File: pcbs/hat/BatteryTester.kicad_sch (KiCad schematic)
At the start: 21 parts

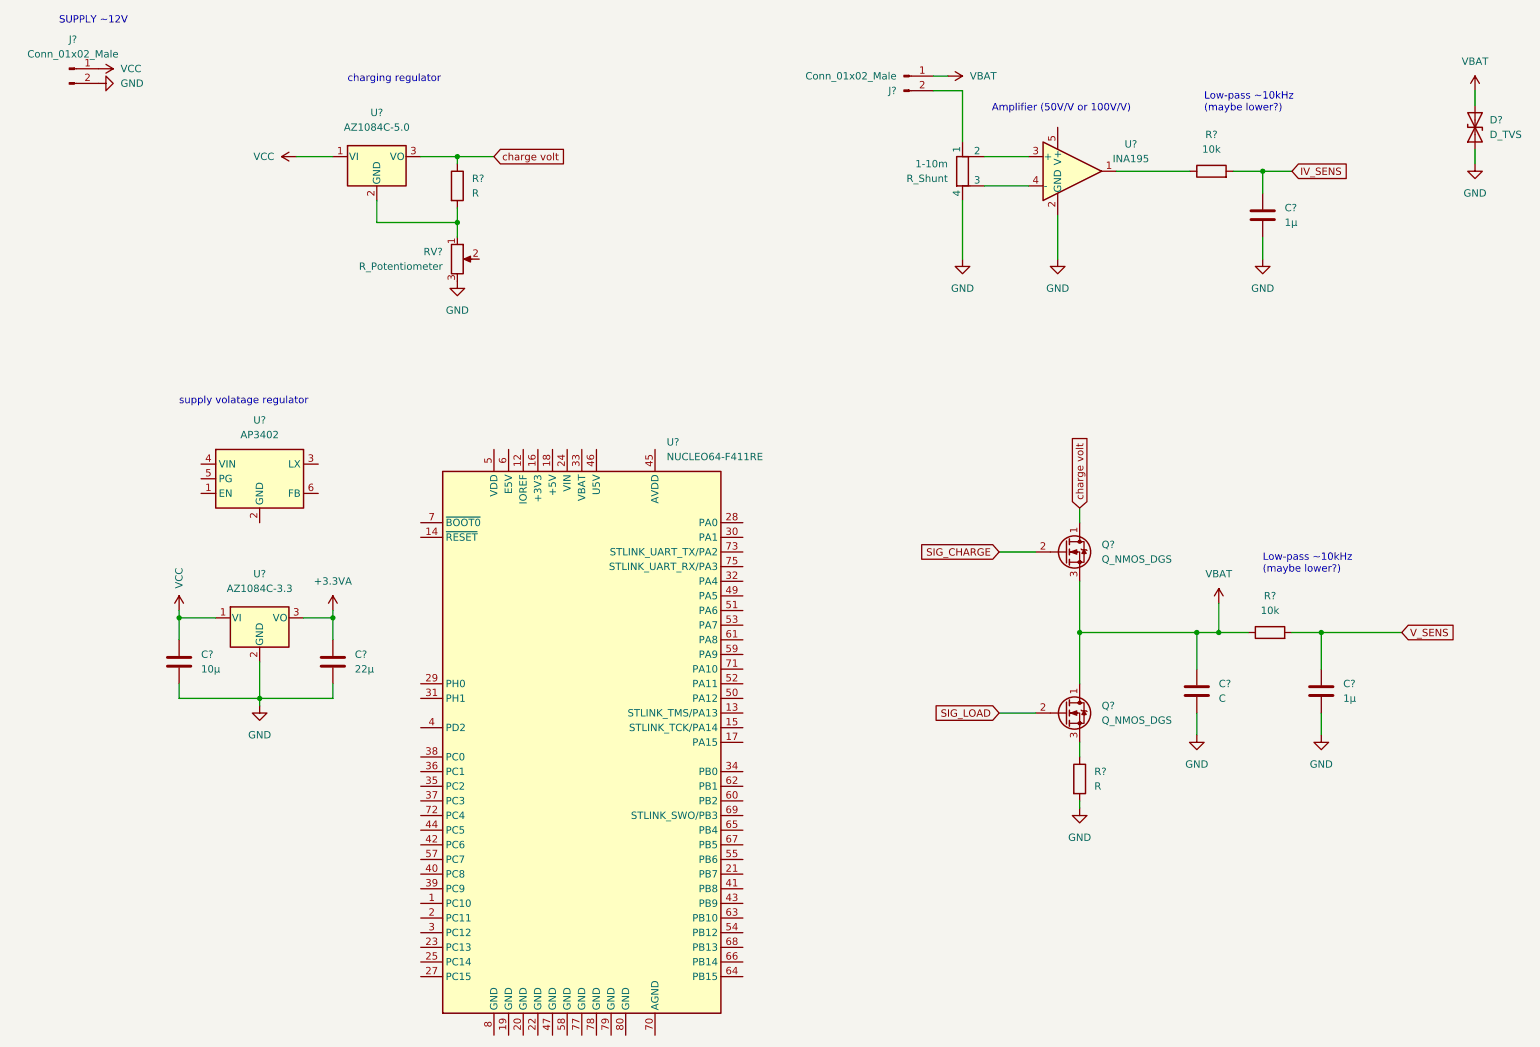
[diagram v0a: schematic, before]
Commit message: add kicad libraries
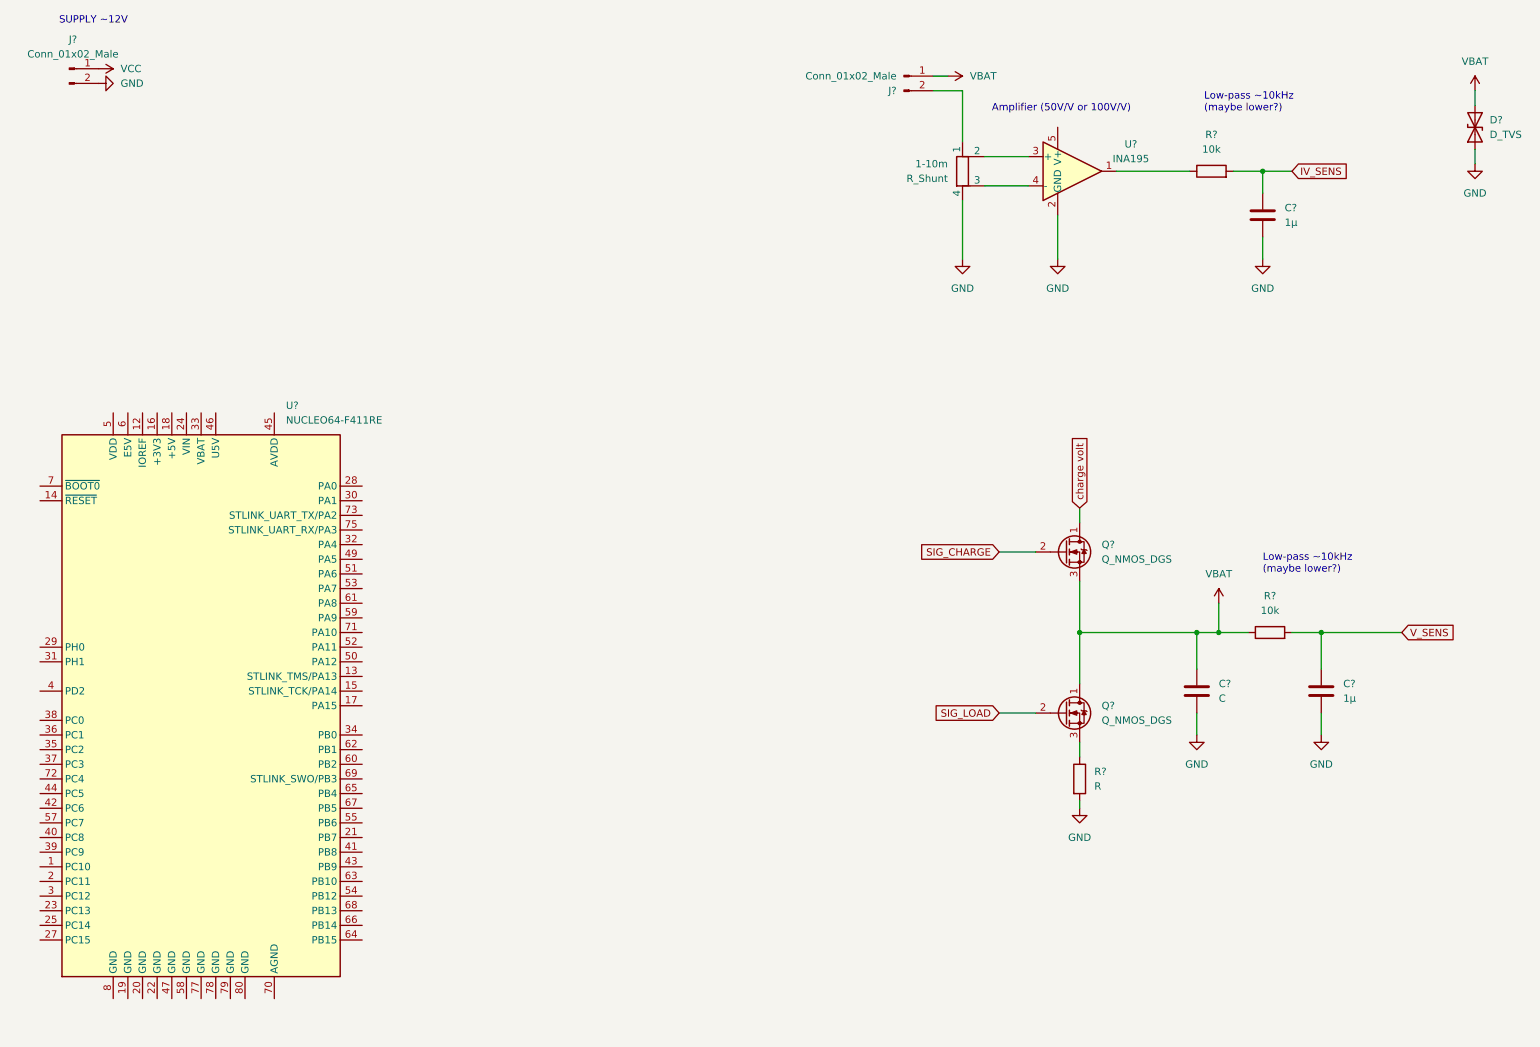
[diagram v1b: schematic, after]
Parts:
- removed C?: 22µ, symbol Device:C
- removed C?: 10µ, symbol Device:C
- removed R?: R, symbol Device:R
- removed RV?: R_Potentiometer, symbol Device:R_Potentiometer
- removed U?: AP3402, Package_TO_SOT_SMD:TSOT-23-6, symbol Regulator_Switching:AP3402
- removed U?: AZ1084C-5.0, Package_TO_SOT_SMD:TO-252-3_TabPin4, symbol Regulator_Linear:KA78M05_TO252
- removed U?: AZ1084C-3.3, Package_TO_SOT_SMD:TO-252-3_TabPin4, symbol Regulator_Linear:KA78M05_TO252
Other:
- note removed: "charging regulator"
- note removed: "supply volatage regulator"
- moved on the sheet: U?

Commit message: setup hierarchy and add Nucleo footprint
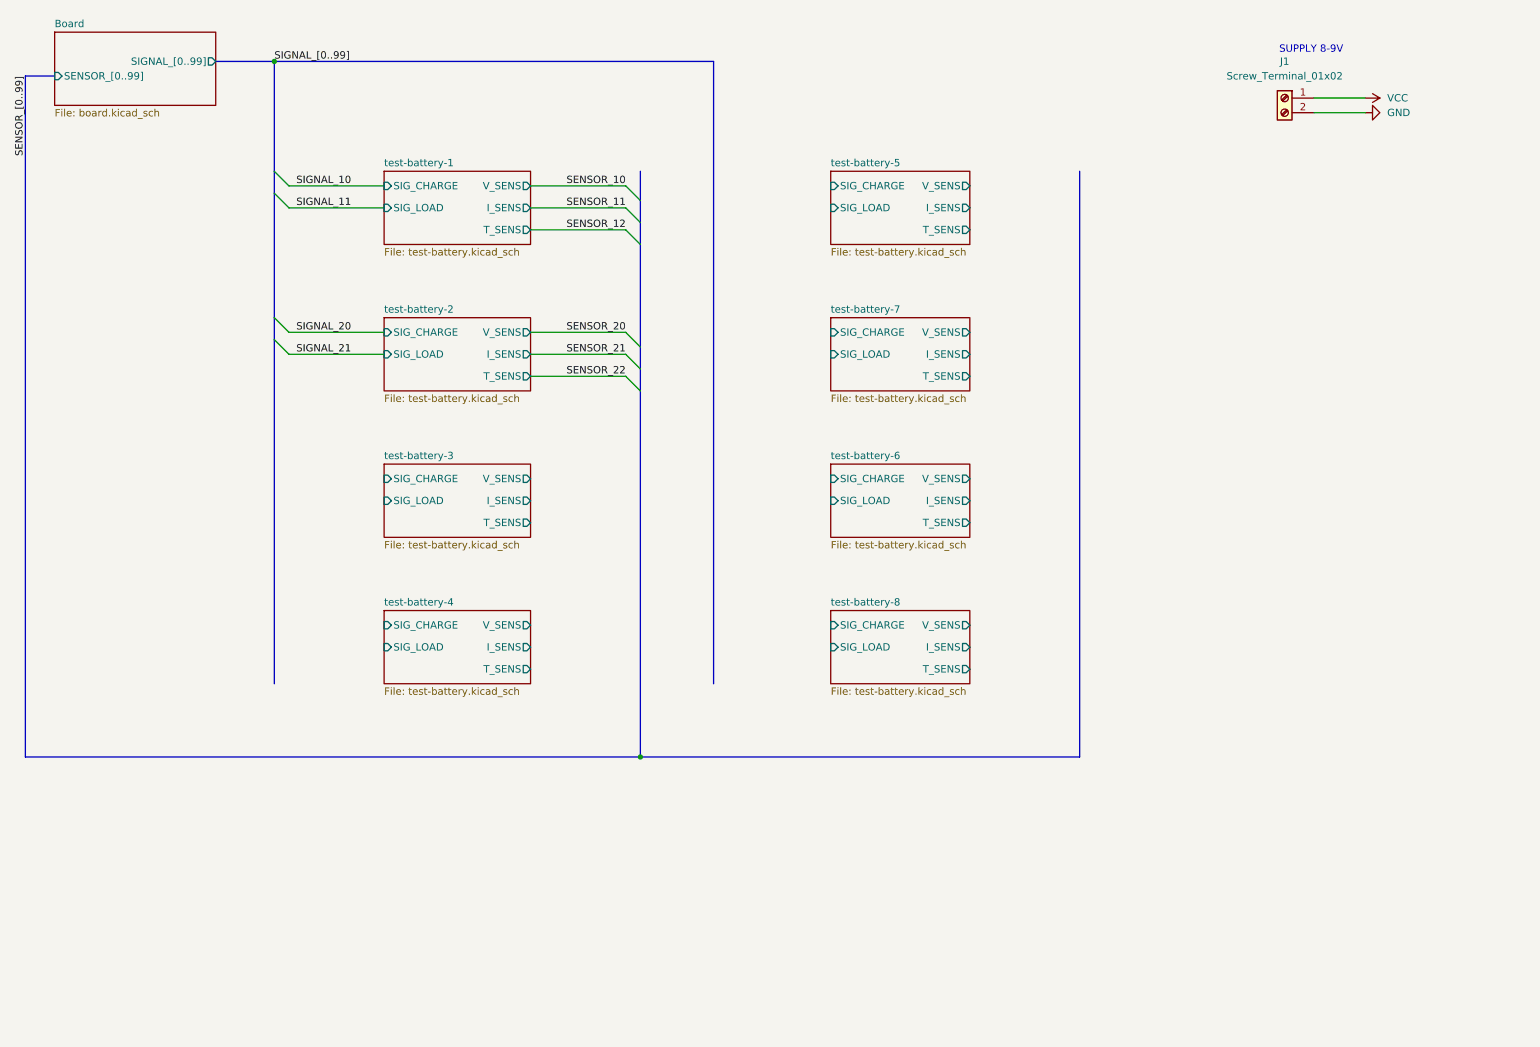
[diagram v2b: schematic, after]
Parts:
- removed 1-10m: R_Shunt, symbol Device:R_Shunt
- removed C? (x2): 1µ, symbol Device:C
- removed C?: C, symbol Device:C
- removed D?: D_TVS, symbol Device:D_TVS
- removed J? (x2): Conn_01x02_Male, symbol Connector:Conn_01x02_Male
- removed Q? (x2): Q_NMOS_DGS, symbol Device:Q_NMOS_DGS
- removed R? (x2): 10k, symbol Device:R
- removed R?: R, symbol Device:R
- removed U?: NUCLEO64-F411RE, Module:ST_Morpho_Connector_144_STLink, symbol MCU_Module:NUCLEO64-F411RE
- removed U?: INA195, Package_TO_SOT_SMD:SOT-23-5, symbol Amplifier_Current:INA195
- added J1: Screw_Terminal_01x02, symbol Connector:Screw_Terminal_01x02
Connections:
- net GND: now also J1.2 (Pin_2)
- net VCC: now also J1.1 (Pin_1)
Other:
- added sheet Board (board.kicad_sch)
- added sheet test-battery-1 (test-battery.kicad_sch)
- added sheet test-battery-2 (test-battery.kicad_sch)
- added sheet test-battery-3 (test-battery.kicad_sch)
- added sheet test-battery-4 (test-battery.kicad_sch)
- added sheet test-battery-5 (test-battery.kicad_sch)
- added sheet test-battery-6 (test-battery.kicad_sch)
- added sheet test-battery-7 (test-battery.kicad_sch)
- added sheet test-battery-8 (test-battery.kicad_sch)
- note added: "SUPPLY 8-9V"
- note removed: "Amplifier (50V/V or 100V/V)"
- note removed: "Low-pass ~10kHz (maybe lower?)"
- note removed: "SUPPLY ~12V"

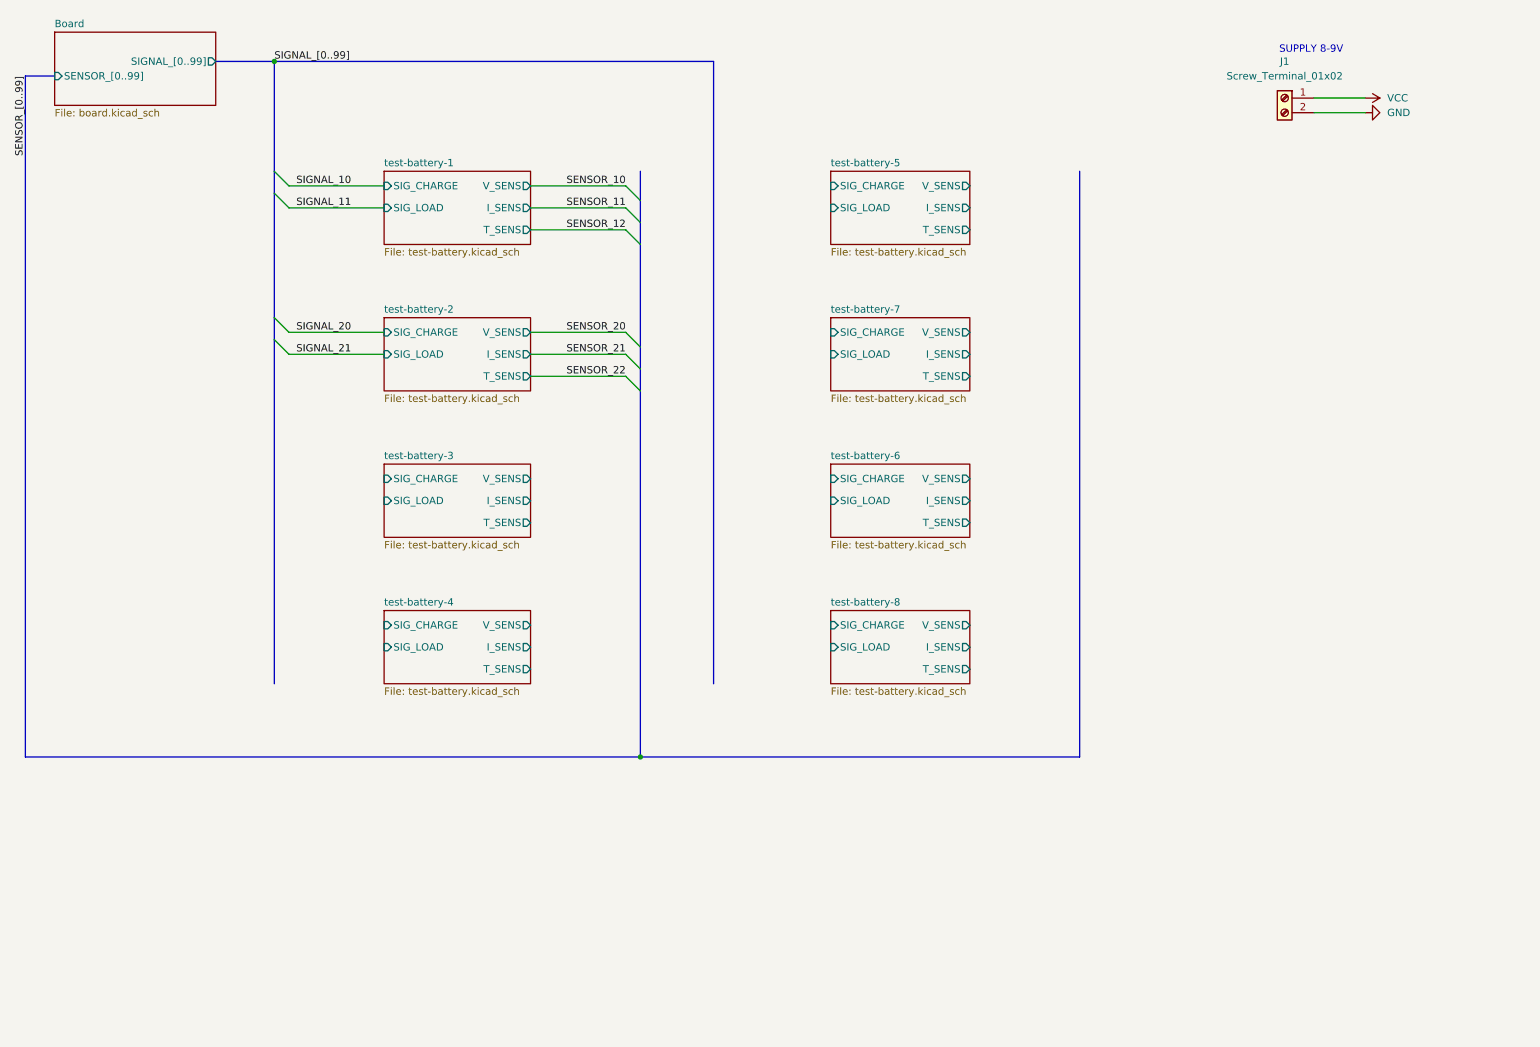
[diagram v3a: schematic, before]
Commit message: add ADCs
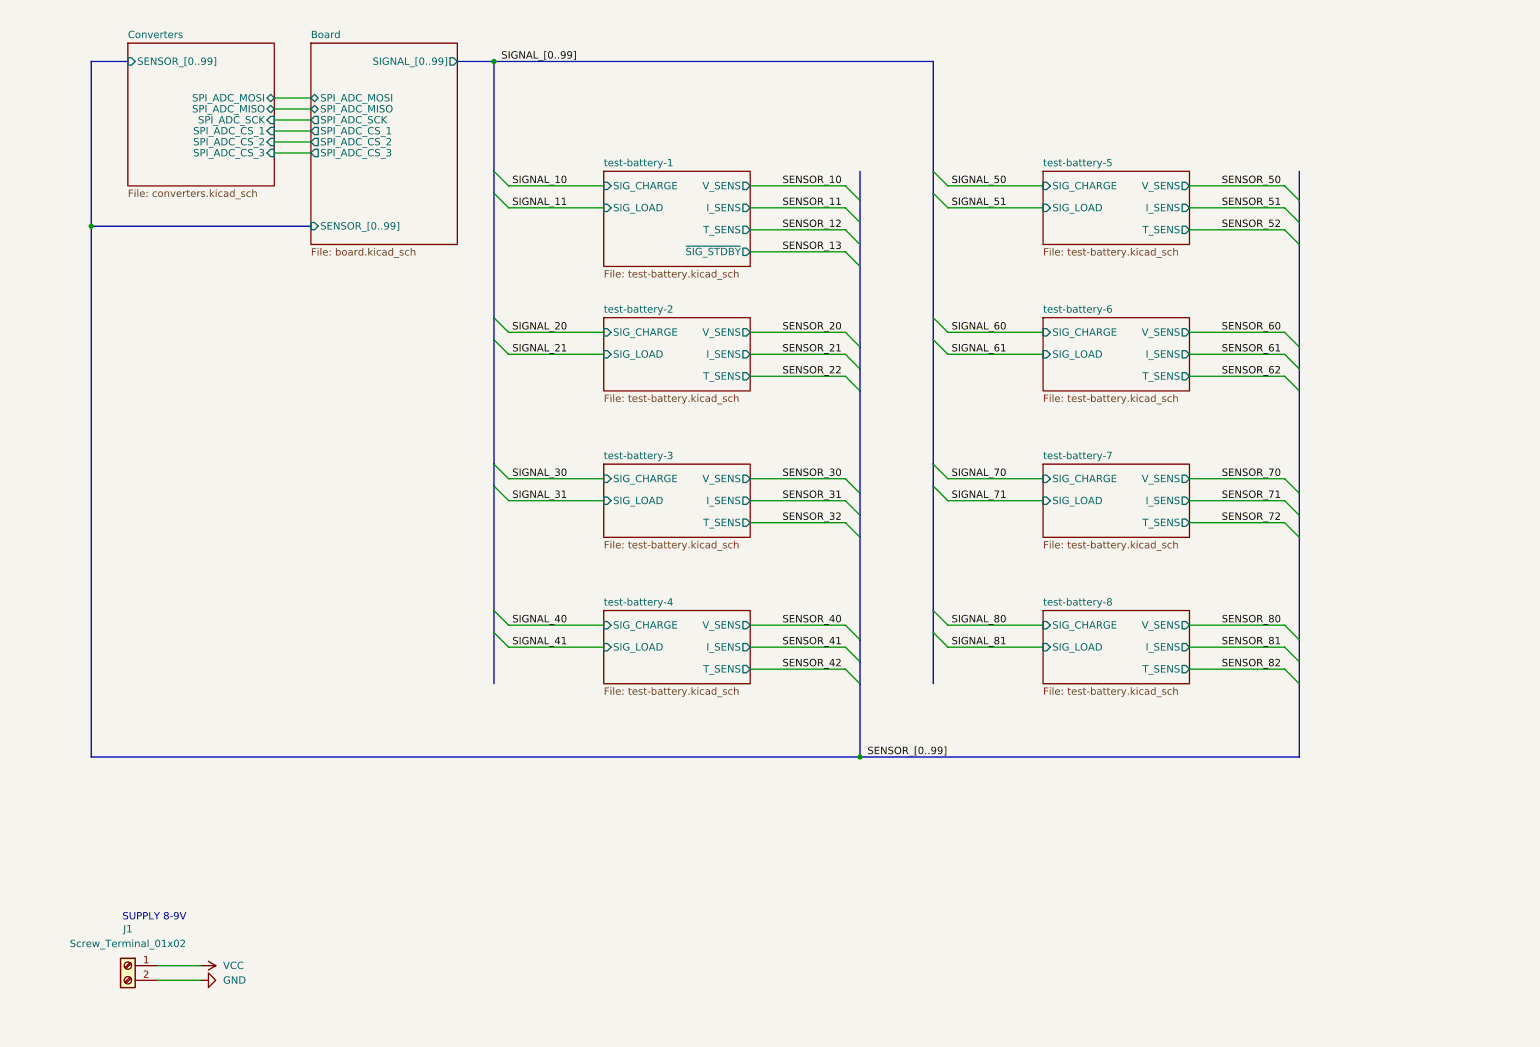
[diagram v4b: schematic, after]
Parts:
- J1: footprint (none) -> TerminalBlock:TerminalBlock_bornier-2_P5.08mm
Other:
- added sheet Converters (converters.kicad_sch)
- sheet Board ports: added SPI_ADC_CS_1, SPI_ADC_CS_2, SPI_ADC_CS_3, SPI_ADC_MISO, SPI_ADC_MOSI, SPI_ADC_SCK; removed none
- sheet test-battery-1 ports: added ~{SIG_STDBY}; removed none
- moved on the sheet: J1

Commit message: more work on charging circuit
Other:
- sheet test-battery-1 ports: added ~{SIG_CHRG_DONE}; removed ~{SIG_STDBY}
- sheet test-battery-2 ports: added ~{SIG_CHRG_DONE}; removed none
- sheet test-battery-3 ports: added ~{SIG_CHRG_DONE}; removed none
- sheet test-battery-4 ports: added ~{SIG_CHRG_DONE}; removed none
- sheet test-battery-5 ports: added ~{SIG_CHRG_DONE}; removed none
- sheet test-battery-6 ports: added ~{SIG_CHRG_DONE}; removed none
- sheet test-battery-7 ports: added ~{SIG_CHRG_DONE}; removed none
- sheet test-battery-8 ports: added ~{SIG_CHRG_DONE}; removed none
